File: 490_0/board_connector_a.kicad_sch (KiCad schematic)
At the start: 14 parts, among them J16 DF40HC(3.0)-100DS-0.4V(58), J17 DF40HC(3.0)-100DS-0.4V(58), J21 TS-102-G-A, Q6 BSS84, SW2 TL1105LF160Q, SW3 TL1105LF160Q, SW4 TL1105LF160Q, SW5 TL1105LF160Q, SW6 TL1105LF160Q, SW7 TL1105LF160Q

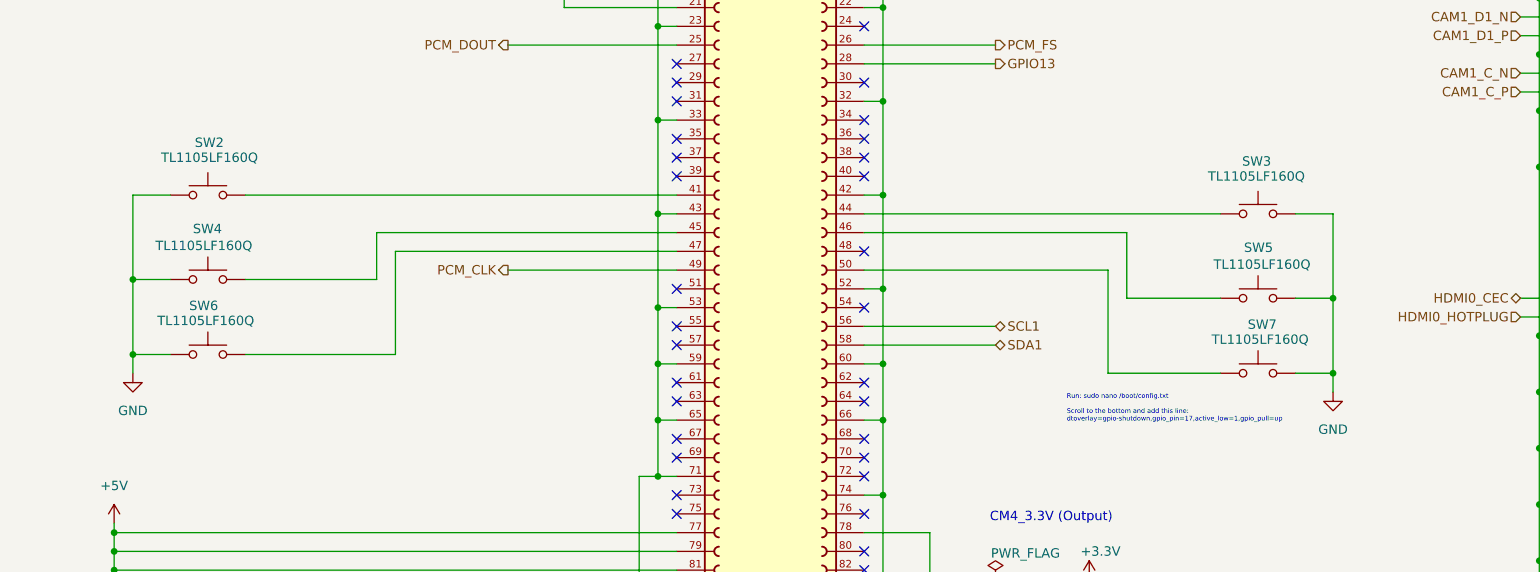
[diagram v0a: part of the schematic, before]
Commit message: Added button debouncing
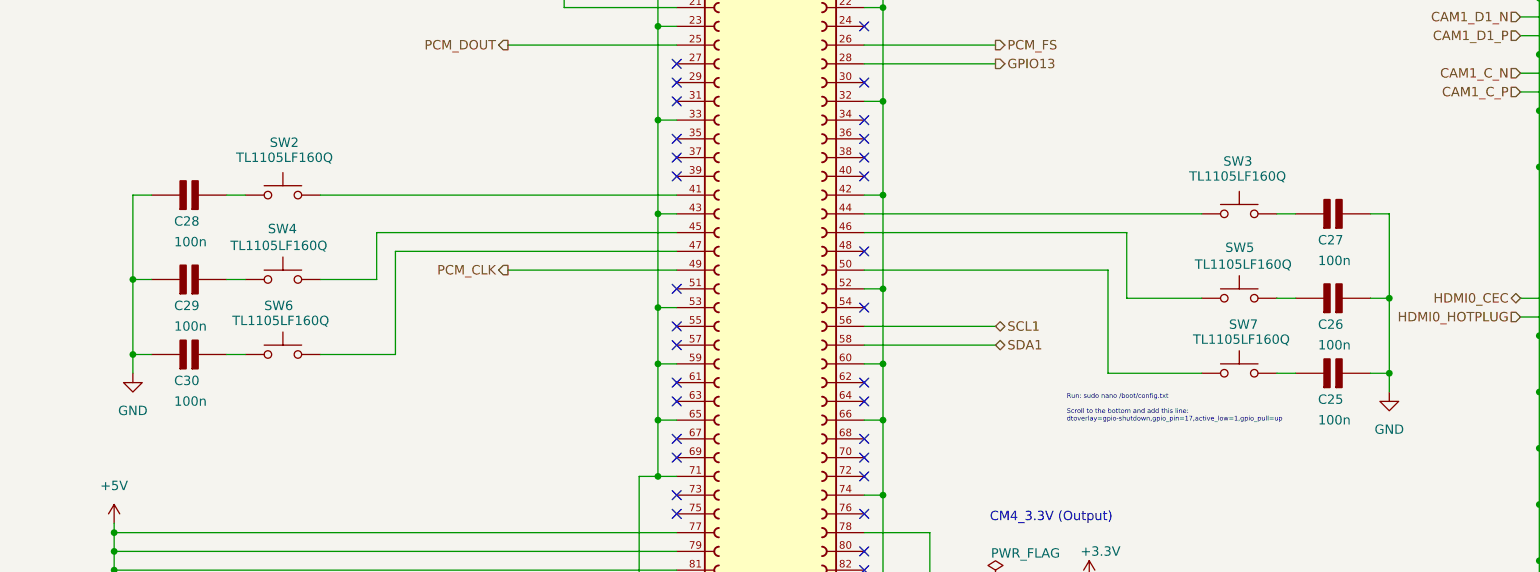
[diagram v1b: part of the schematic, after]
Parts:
- added C25, C26, C27, C28, C29, C30: 100n, Capacitor_SMD:C_0603_1608Metric, symbol PCM_Elektuur:C
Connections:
- net GND: now also C25.2 (-), C26.2 (-), C27.2 (-), C28.1 (+), C29.1 (+), C30.1 (+); no longer SW2.1, SW3.1, SW4.1, SW5.1, SW6.1, SW7.1
- new net: C30.2 (-), SW6.1
- new net: C26.1 (+), SW5.1
- new net: C27.1 (+), SW3.1
- new net: C25.1 (+), SW7.1
- new net: C28.2 (-), SW2.1
- new net: C29.2 (-), SW4.1
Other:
- moved on the sheet: SW2, SW3, SW4, SW5, SW6, SW7

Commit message: Added side B for SW1
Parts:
- C25, C26, C27, C28, C29, C30: symbol PCM_Elektuur:C -> capstone_parts:C
- D16, D17: symbol Device:LED -> capstone_parts:LED
- J16: symbol capstone_parts:DF40C-100DS-0.4V_51_ -> capstone_parts:DF40C-100DS-0.4V_51__1
- J21: symbol PCM_4ms_Connector:Conn_01x02 -> capstone_parts:Conn_01x02
- Q6: symbol Simulation_SPICE:PMOS -> capstone_parts:PMOS
- R37, R44: symbol Device:R -> capstone_parts:R
- SW2, SW3, SW4, SW5, SW6, SW7: symbol Switch:SW_Push -> capstone_parts:SW_Push
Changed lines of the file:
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@@
 	(symbol
 		(lib_name "DF40C-100DS-0.4V_51__1")
-		(lib_id "capstone_parts:DF40C-100DS-0.4V_51_")
+		(lib_id "capstone_parts:DF40C-100DS-0.4V_51__1")
 		(at 111.76 87.63 0)
 		(unit 1)
@@
 	)
 	(symbol
-		(lib_id "Simulation_SPICE:PMOS")
+		(lib_id "capstone_parts:PMOS")
 		(at 71.12 162.56 180)
 		(unit 1)
@@
 	)
 	(symbol
-		(lib_id "Switch:SW_Push")
+		(lib_id "capstone_parts:SW_Push")
 		(at 45.72 99.06 0)
 		(unit 1)
@@
 	)
 	(symbol
-		(lib_id "Switch:SW_Push")
+		(lib_id "capstone_parts:SW_Push")
 		(at 175.26 91.44 0)
 		(mirror y)
@@
 	)
 	(symbol
-		(lib_id "Switch:SW_Push")
+		(lib_id "capstone_parts:SW_Push")
 		(at 175.26 80.01 0)
 		(mirror y)
@@
 	)
 	(symbol
-		(lib_id "Device:LED")
+		(lib_id "capstone_parts:LED")
 		(at 83.82 45.72 90)
 		(unit 1)
@@
 	)
 	(symbol
-		(lib_id "PCM_Elektuur:C")
+		(lib_id "capstone_parts:C")
 		(at 187.96 101.6 90)
 		(unit 1)
@@
 	)
 	(symbol
-		(lib_id "PCM_Elektuur:C")
+		(lib_id "capstone_parts:C")
 		(at 187.96 91.44 90)
 		(unit 1)
@@
 	)
 	(symbol
-		(lib_id "PCM_Elektuur:C")
+		(lib_id "capstone_parts:C")
 		(at 187.96 80.01 90)
 		(unit 1)
@@
 	)
 	(symbol
-		(lib_id "Device:R")
+		(lib_id "capstone_parts:R")
 		(at 68.58 173.99 0)
 		(mirror y)
@@
 	)
 	(symbol
-		(lib_id "Switch:SW_Push")
+		(lib_id "capstone_parts:SW_Push")
 		(at 45.72 77.47 0)
 		(unit 1)
@@
 	)
 	(symbol
-		(lib_id "Device:R")
+		(lib_id "capstone_parts:R")
 		(at 83.82 35.56 0)
 		(mirror y)
@@
 	)
 	(symbol
-		(lib_id "Switch:SW_Push")
+		(lib_id "capstone_parts:SW_Push")
 		(at 175.26 101.6 0)
 		(mirror y)
@@
 	)
 	(symbol
-		(lib_id "PCM_Elektuur:C")
+		(lib_id "capstone_parts:C")
 		(at 33.02 88.9 90)
 		(unit 1)
@@
 	)
 	(symbol
-		(lib_id "PCM_Elektuur:C")
+		(lib_id "capstone_parts:C")
 		(at 33.02 77.47 90)
 		(unit 1)
@@
 	)
 	(symbol
-		(lib_id "Device:LED")
+		(lib_id "capstone_parts:LED")
 		(at 68.58 184.15 90)
 		(unit 1)
@@
 	)
 	(symbol
-		(lib_id "PCM_4ms_Connector:Conn_01x02")
+		(lib_id "capstone_parts:Conn_01x02")
 		(at 50.8 182.88 180)
 		(unit 1)
@@
 	)
 	(symbol
-		(lib_id "Switch:SW_Push")
+		(lib_id "capstone_parts:SW_Push")
 		(at 45.72 88.9 0)
 		(unit 1)
@@
 	)
 	(symbol
-		(lib_id "PCM_Elektuur:C")
+		(lib_id "capstone_parts:C")
 		(at 33.02 99.06 90)
 		(unit 1)

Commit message: Rerouted + external coponents update
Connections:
- net GPIO13: no longer names the net of J16.28
- no-connect marks 104 -> 105
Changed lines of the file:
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@@
 	)
 	(no_connect
+		(at 124.46 59.69)
+	)
+	(no_connect
 		(at 218.44 40.64)
 	)
@@
 	(wire
 		(pts
-			(xy 142.24 59.69) (xy 124.46 59.69)
-		)
-		(stroke
-			(width 0)
-			(type default)
-		)
-	)
-	(wire
-		(pts
 			(xy 22.86 133.35) (xy 22.86 135.89)
 		)
@@
 		)
 	)
-	(hierarchical_label "GPIO13"
-		(shape output)
-		(at 142.24 59.69 0)
-		(effects
-			(font
-				(size 1.27 1.27)
-			)
-			(justify left)
-		)
-	)

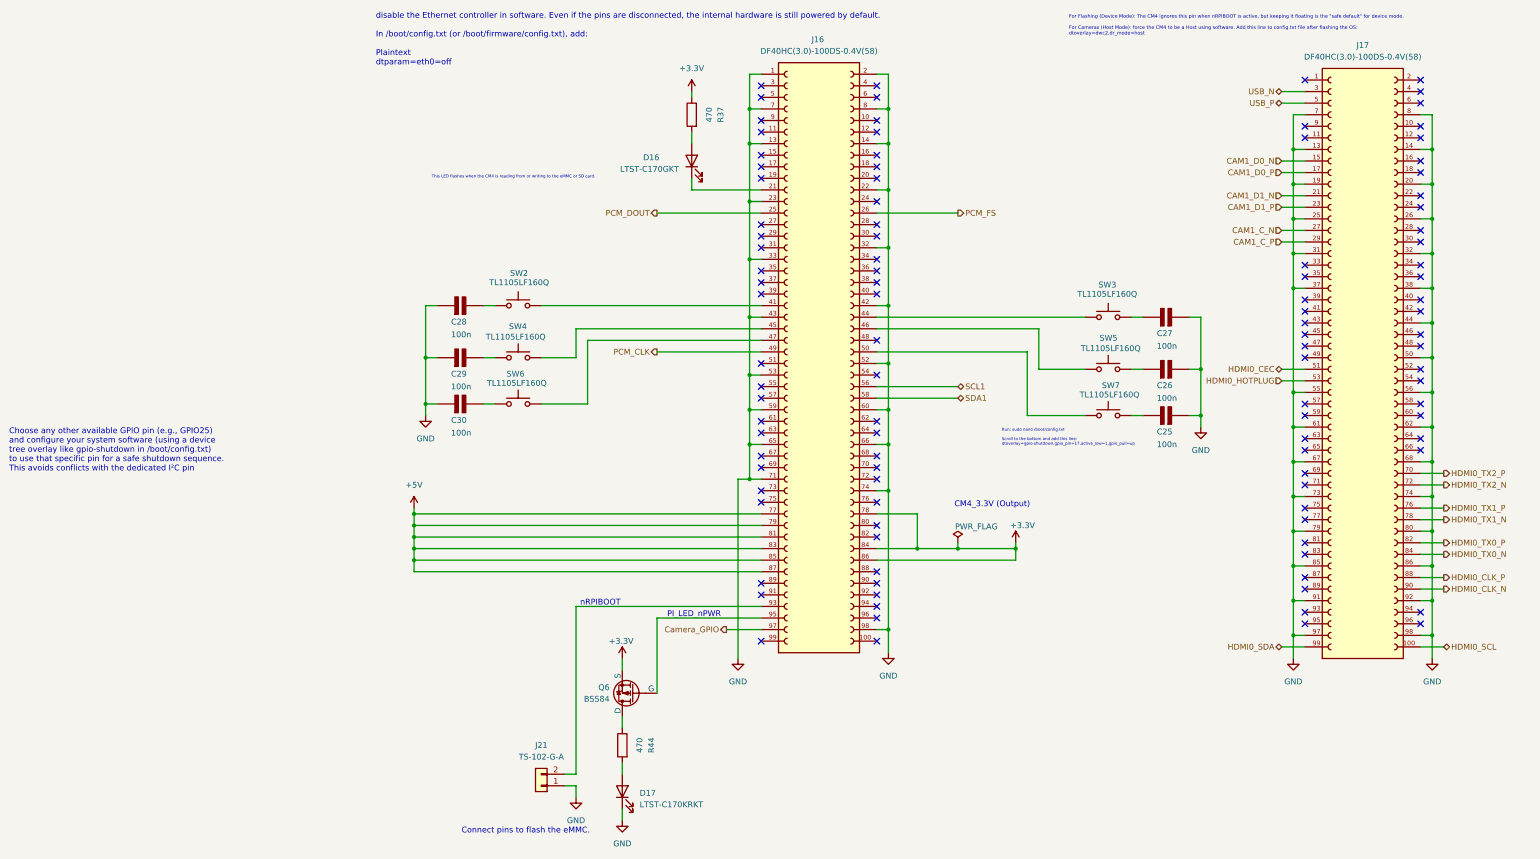
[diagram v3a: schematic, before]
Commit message: Fixed button debouncing
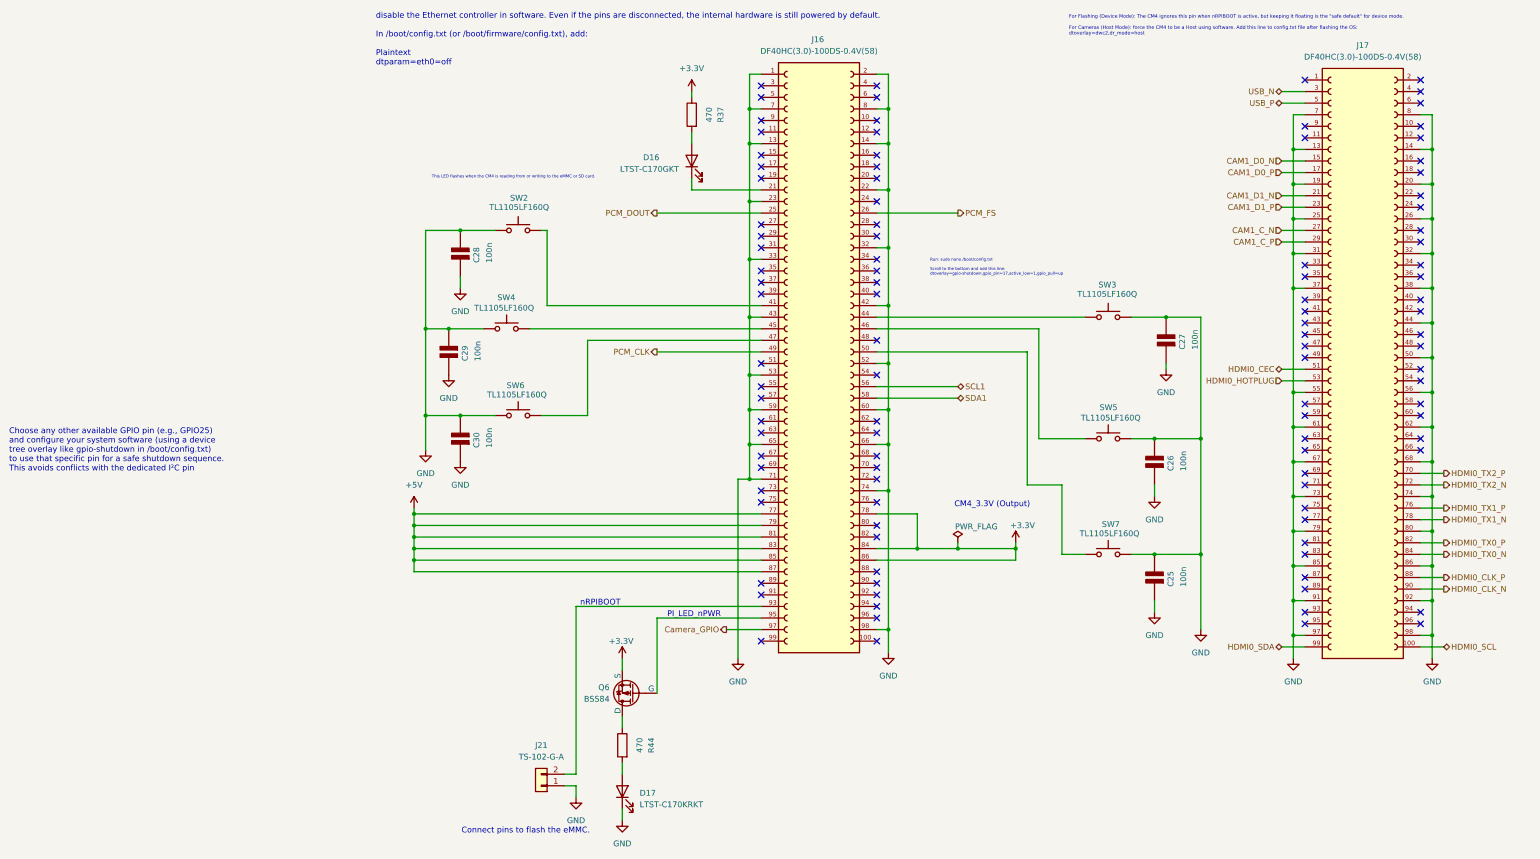
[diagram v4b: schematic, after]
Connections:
- net GND: now also C25.1 (+), C26.1 (+), C27.1 (+), C28.2 (-), C29.2 (-), C30.2 (-), SW2.1, SW3.1, SW4.1, SW5.1, SW6.1, SW7.1
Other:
- moved on the sheet: C25, C26, C27, C28, C29, C30, SW2, SW4, SW5, SW6, SW7

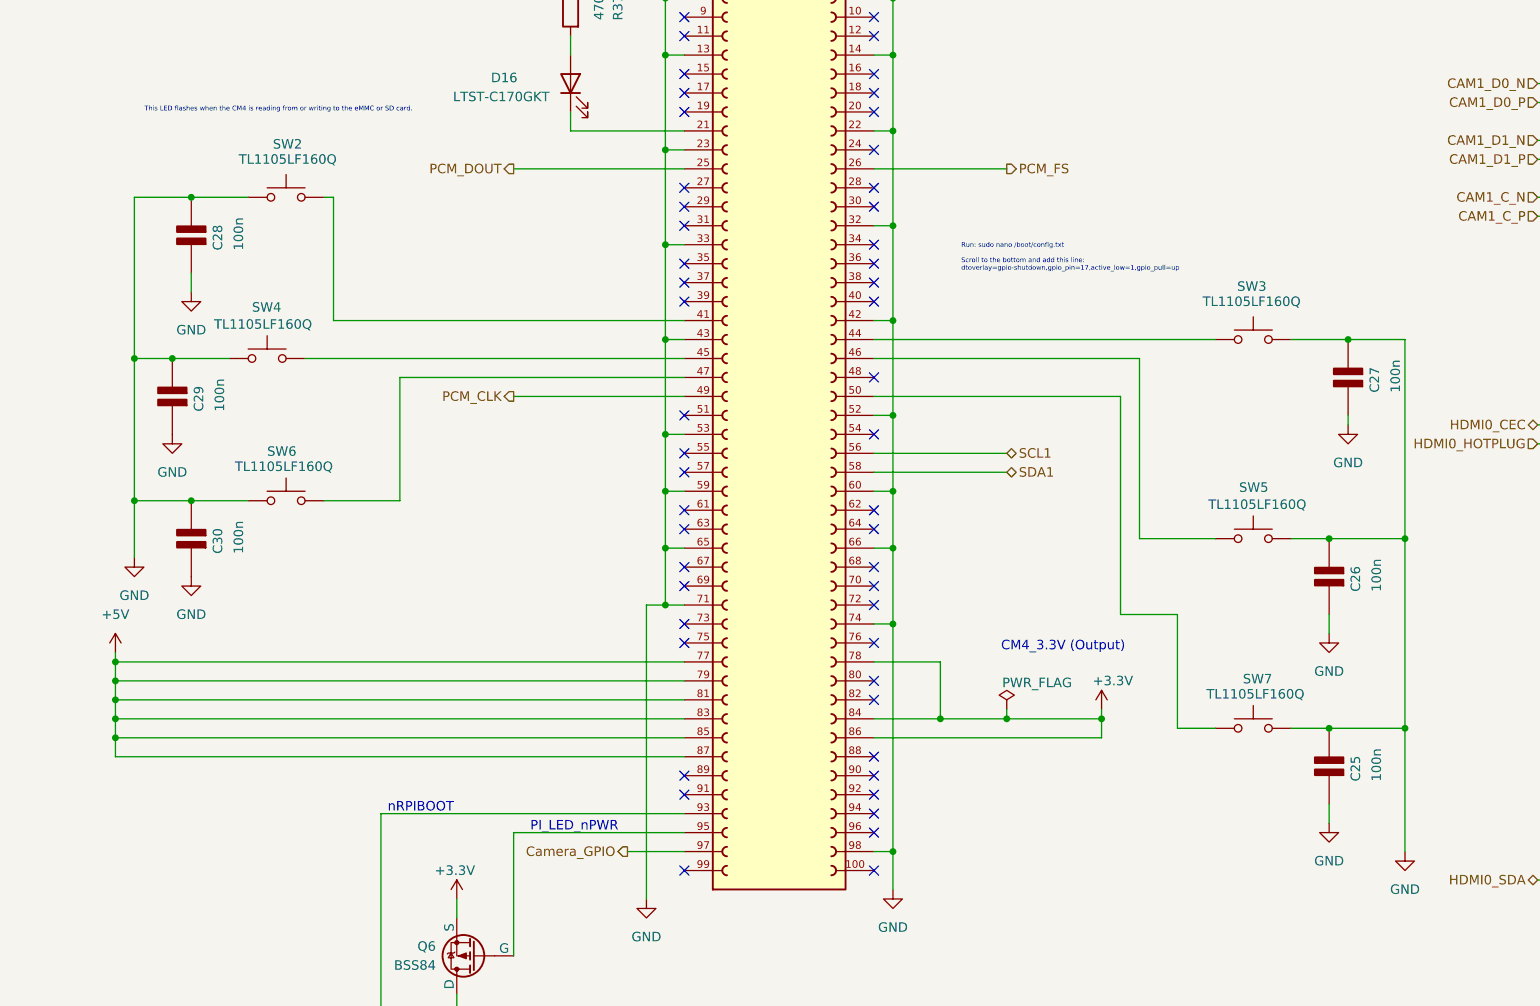
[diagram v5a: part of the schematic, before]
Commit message: Button debouncing fix
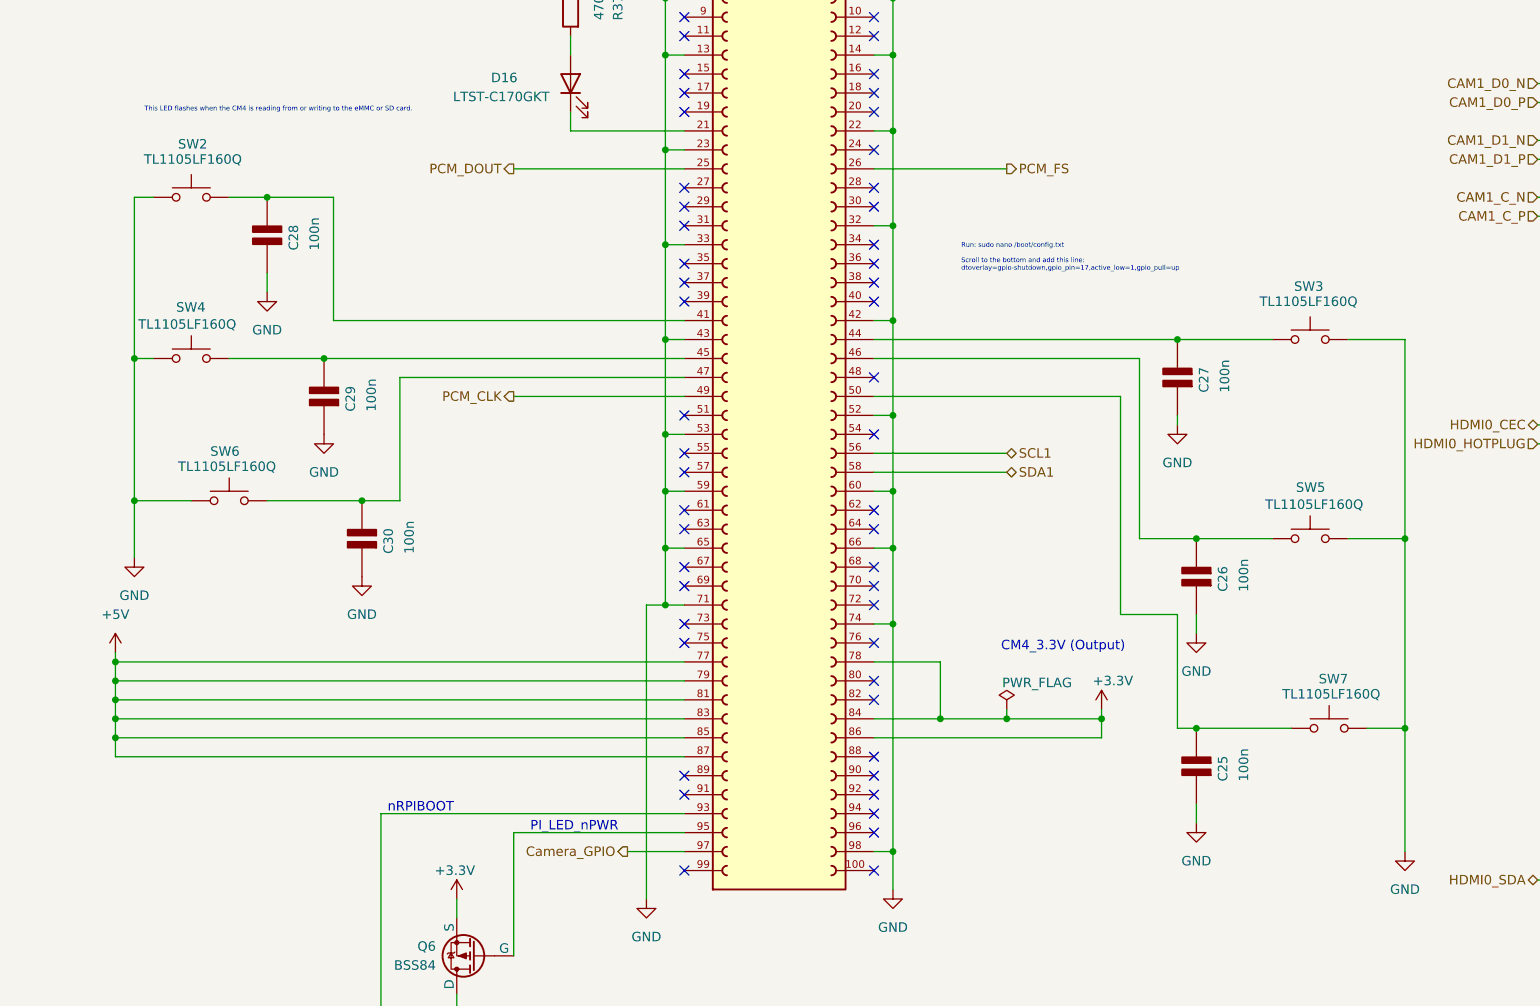
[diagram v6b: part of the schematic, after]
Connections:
- net GND: no longer C25.2 (-), C26.2 (-), C27.2 (-), C28.2 (-), C29.2 (-), C30.2 (-)
- net at J16.41, SW2.2: now also C28.2 (-)
- net at J16.44, SW3.2: now also C27.2 (-)
- net at J16.45, SW4.2: now also C29.2 (-)
- net at J16.46, SW5.2: now also C26.2 (-)
- net at J16.47, SW6.2: now also C30.2 (-)
- net at J16.50, SW7.2: now also C25.2 (-)
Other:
- moved on the sheet: C25, C26, C27, C28, C29, C30, SW2, SW3, SW4, SW5, SW6, SW7
